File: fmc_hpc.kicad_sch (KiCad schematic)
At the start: 33 parts

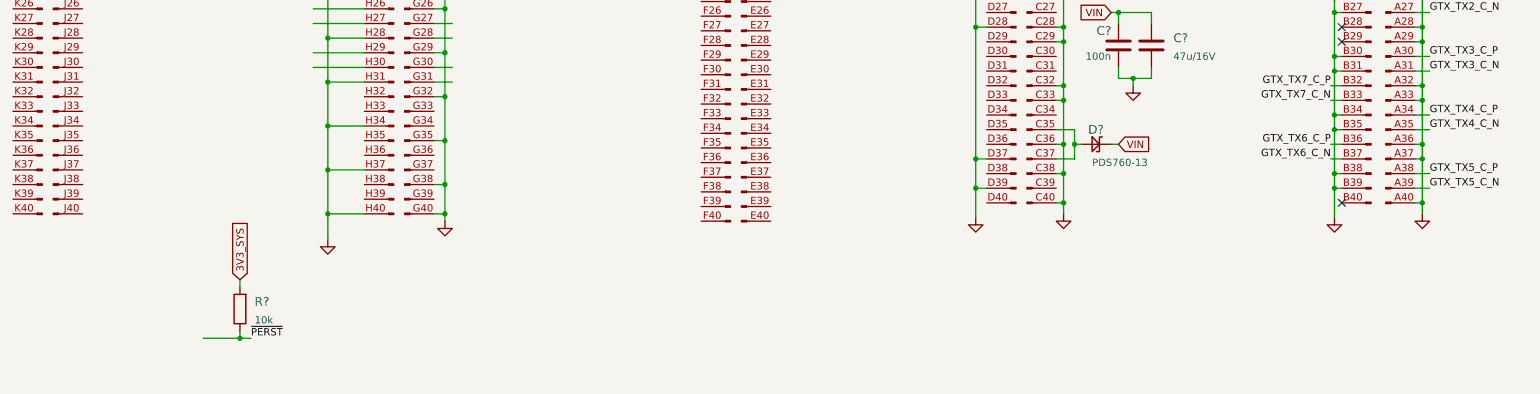
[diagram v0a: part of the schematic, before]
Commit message: Add power cycling circuitry
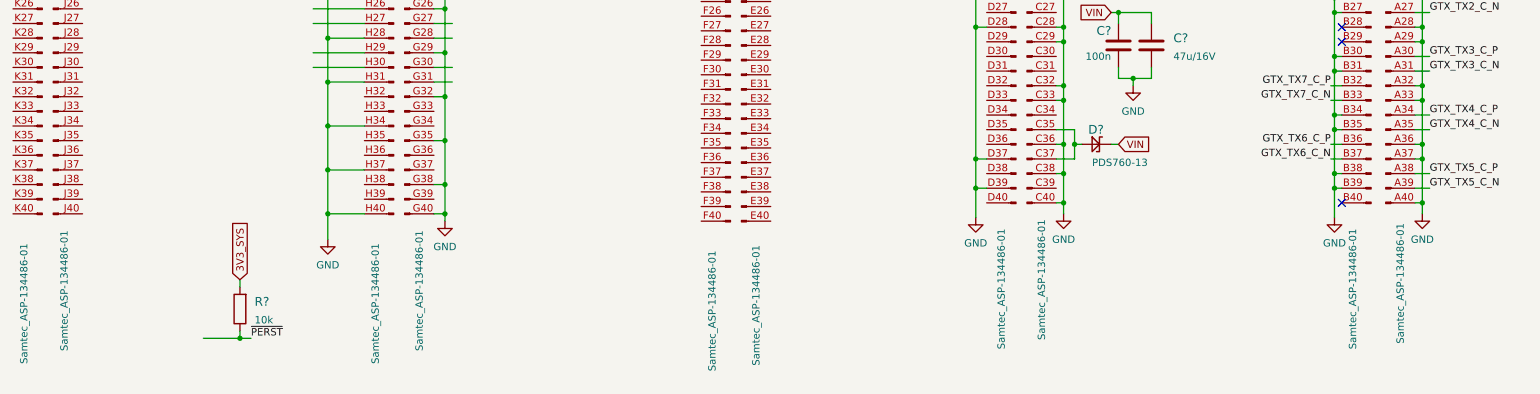
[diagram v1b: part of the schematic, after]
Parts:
- C? (x16): value (none) -> C_100n_0402; footprint (none) -> antmicro-footprints:0402-cap
- C?: value (none) -> C_100n_0201; footprint (none) -> antmicro-footprints:0201-res
- C?: value (none) -> C_47u_16V_1206; footprint (none) -> antmicro-footprints:1206-cap
- D?: value (none) -> PDS760-13; footprint (none) -> data-center-dram-tester-footprints:PDS760-13
- J? (x10): value (none) -> Samtec_ASP-134486-01
- R? (x2): value (none) -> R_33R_0402; footprint (none) -> antmicro-footprints:0402-res
- R?: value (none) -> R_10k_0402; footprint (none) -> antmicro-footprints:0402-res
- R?: value (none) -> R_100k_0402; footprint (none) -> antmicro-footprints:0402-res

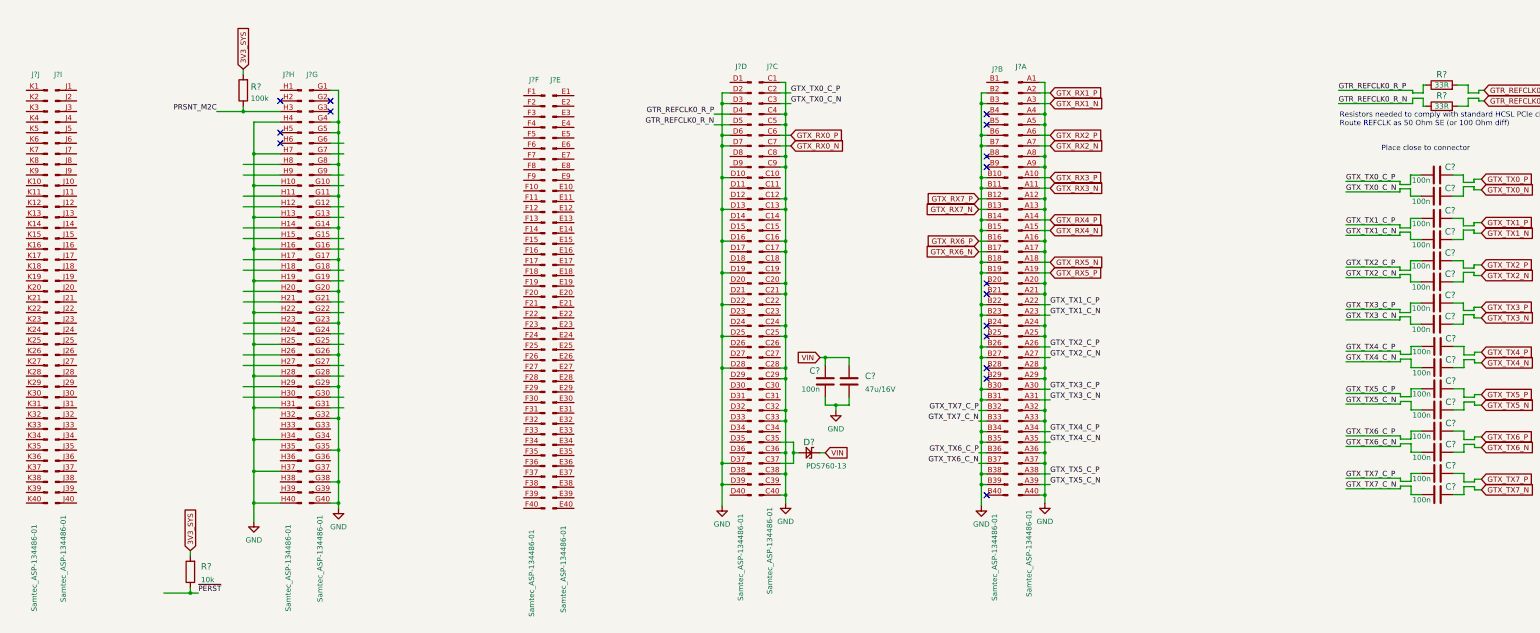
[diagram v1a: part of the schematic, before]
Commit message: Connect ETH mux, connect AUX_JTAG to FMC connector, add RC filter for HOT_SWAP_BUTTON signal
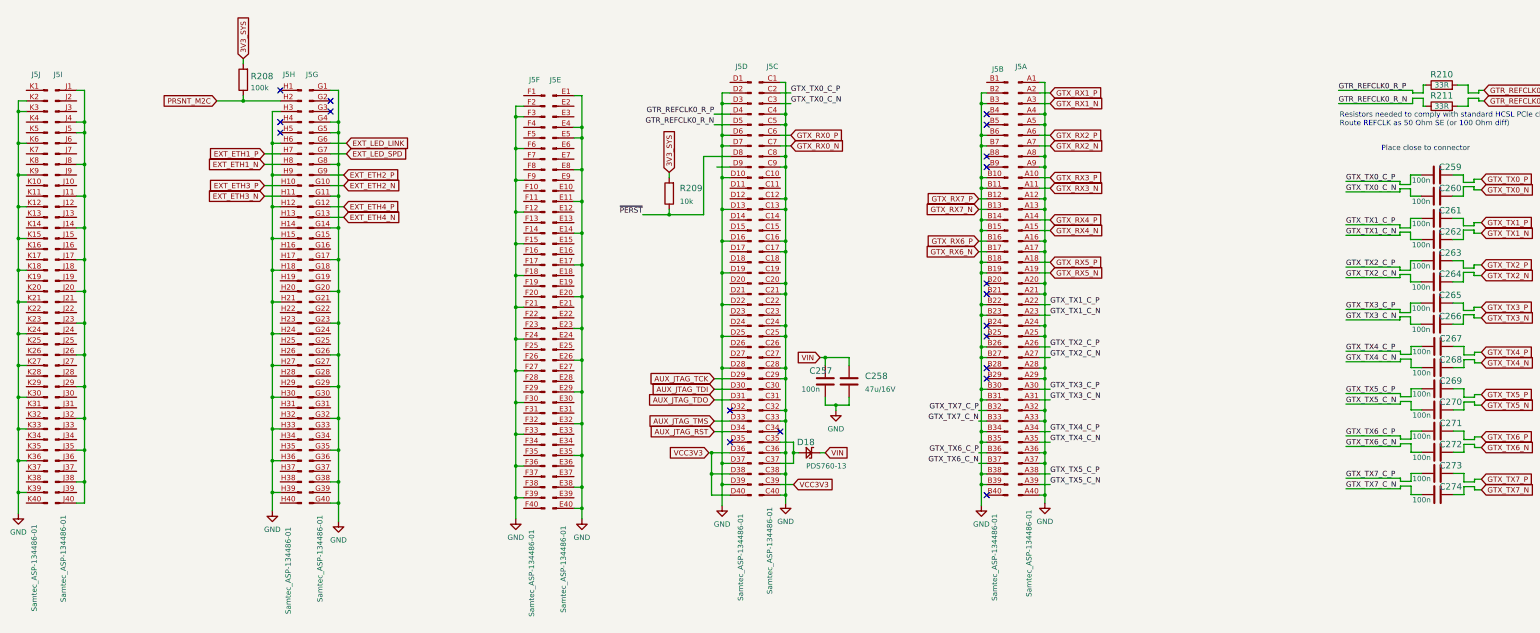
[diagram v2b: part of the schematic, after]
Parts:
- gave numbers to parts that had none: 24
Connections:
- net GND: now also J5.E1 (Pin_1), J5.E11 (Pin_11), J5.E14 (Pin_14), J5.E17 (Pin_17), J5.E20 (Pin_20), J5.E23 (Pin_23), J5.E26 (Pin_26), J5.E29 (Pin_29), J5.E32 (Pin_32), J5.E35 (Pin_35), J5.E38 (Pin_38), J5.E4 (Pin_4), J5.E40 (Pin_40), J5.E5 (Pin_5), J5.E8 (Pin_8), J5.F12 (Pin_12), J5.F15 (Pin_15), J5.F18 (Pin_18), J5.F2 (Pin_2), J5.F21 (Pin_21), J5.F24 (Pin_24), J5.F27 (Pin_27), J5.F3 (Pin_3), J5.F30 (Pin_30), J5.F33 (Pin_33), J5.F36 (Pin_36), J5.F39 (Pin_39), J5.F6 (Pin_6), J5.F9 (Pin_9), J5.H12 (Pin_12), J5.H15 (Pin_15), J5.H18 (Pin_18), J5.H21 (Pin_21), J5.H24 (Pin_24), J5.H27 (Pin_27), J5.H3 (Pin_3), J5.H30 (Pin_30), J5.H33 (Pin_33), J5.H36 (Pin_36), J5.H39 (Pin_39), J5.H6 (Pin_6), J5.H9 (Pin_9), J5.K12 (Pin_12), J5.K15 (Pin_15), J5.K18 (Pin_18), J5.K2 (Pin_2), J5.K21 (Pin_21), J5.K24 (Pin_24), J5.K27 (Pin_27), J5.K3 (Pin_3), J5.K30 (Pin_30), J5.K33 (Pin_33), J5.K36 (Pin_36), J5.K39 (Pin_39), J5.K6 (Pin_6), J5.K9 (Pin_9); no longer J5.H10 (Pin_10), J5.H13 (Pin_13), J5.H16 (Pin_16), J5.H19 (Pin_19), J5.H22 (Pin_22), J5.H25 (Pin_25), J5.H28 (Pin_28), J5.H31 (Pin_31), J5.H34 (Pin_34), J5.H37 (Pin_37), J5.H4 (Pin_4), J5.H40 (Pin_40), J5.H7 (Pin_7)
- net GTX_RX5_N: now also J5.A19 (Pin_19); no longer J5.A18 (Pin_18)
- net GTX_RX5_P: now also J5.A18 (Pin_18); no longer J5.A19 (Pin_19)
- net PRSNT_M2C: now also J5.H2 (Pin_2); no longer J5.H3 (Pin_3)
- net ~{PERST}: now also J5.D8 (Pin_8)
- net EXT_ETH3_N: now reaches J5.H11 (Pin_11)
- net EXT_ETH1_N: now reaches J5.H8 (Pin_8)
- net AUX_JTAG_TCK: now reaches J5.D29 (Pin_29)
- net AUX_JTAG_TDI: now reaches J5.D30 (Pin_30)
- net AUX_JTAG_TDO: now reaches J5.D31 (Pin_31)
- net AUX_JTAG_TMS: now reaches J5.D33 (Pin_33)
- net AUX_JTAG_RST: now reaches J5.D34 (Pin_34)
- net VCC3V3: now reaches J5.D36 (Pin_36)
- net VCC3V3: now also J5.C39 (Pin_39), J5.D38 (Pin_38), J5.D40 (Pin_40)
- net at J5.J1 (Pin_1): now also J5.J11 (Pin_11), J5.J14 (Pin_14), J5.J17 (Pin_17), J5.J20 (Pin_20), J5.J23 (Pin_23), J5.J26 (Pin_26), J5.J29 (Pin_29), J5.J32 (Pin_32), J5.J35 (Pin_35), J5.J38 (Pin_38), J5.J4 (Pin_4), J5.J40 (Pin_40), J5.J5 (Pin_5), J5.J8 (Pin_8)
- net EXT_ETH2_N: now reaches J5.G10 (Pin_10)
- net EXT_ETH4_P: now reaches J5.G12 (Pin_12)
- net EXT_ETH4_N: now reaches J5.G13 (Pin_13)
- net EXT_LED_LINK: now reaches J5.G6 (Pin_6)
- net EXT_LED_SPD: now reaches J5.G7 (Pin_7)
- net EXT_ETH2_P: now reaches J5.G9 (Pin_9)
- new net EXT_ETH1_P: J5.H7 (Pin_7)
- new net EXT_ETH3_P: J5.H10 (Pin_10)
- no-connect marks 16 -> 19
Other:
- moved on the sheet: R208, R209

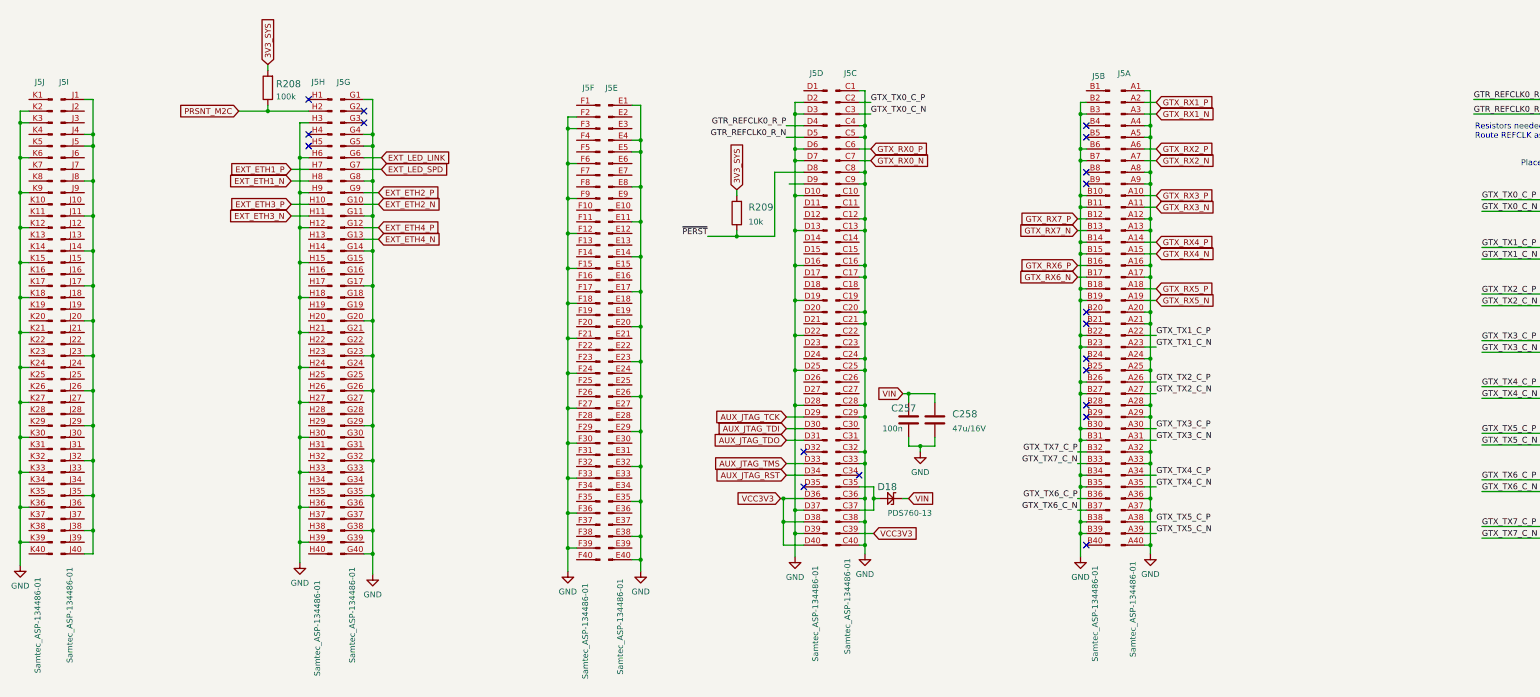
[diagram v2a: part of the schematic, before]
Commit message: Replaced JTAG to surface mount, Update FMC HPC socket
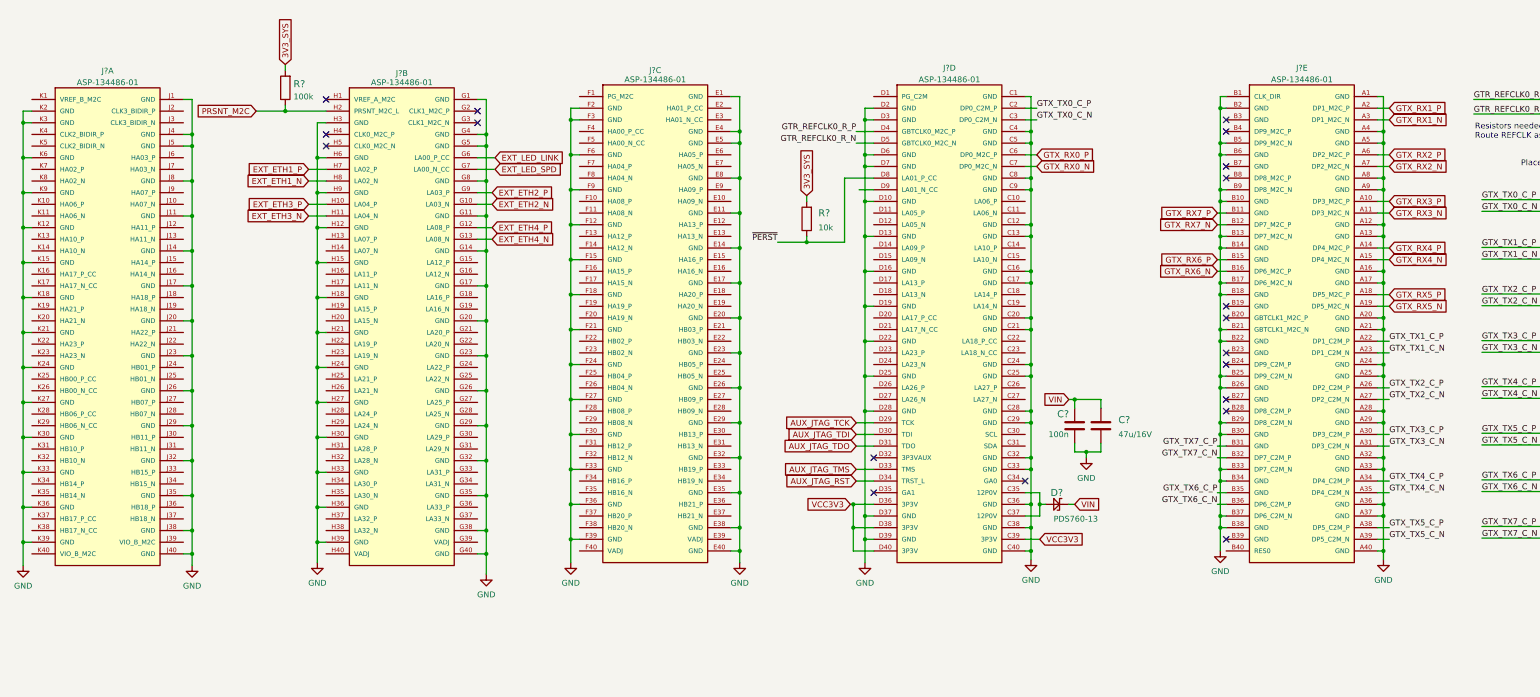
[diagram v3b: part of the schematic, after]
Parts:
- removed C257: C_100n_0201, antmicro-footprints:0201-res, symbol antmicroCapacitorsmisc:C_100n_0201
- removed C258: C_47u_16V_1206, antmicro-footprints:1206-cap, symbol antmicroCapacitorsmisc:C_47u_16V_1206
- removed D18: PDS760-13, data-center-dram-tester-footprints:PDS760-13, symbol data-center-dram-tester:PDS760-13
- removed J5: Samtec_ASP-134486-01, symbol Connector:Samtec_ASP-134486-01
- removed R208: R_100k_0402, antmicro-footprints:0402-res, symbol antmicroResistors0402:R_100k_0402
- removed R209: R_10k_0402, antmicro-footprints:0402-res, symbol antmicroResistors0402:R_10k_0402
- added C?: C_100n_0201, antmicro-footprints:0201-res, symbol antmicroCapacitorsmisc:C_100n_0201
- added C?: C_47u_16V_1206, antmicro-footprints:1206-cap, symbol antmicroCapacitorsmisc:C_47u_16V_1206
- added D?: PDS760-13, data-center-dram-tester-footprints:PDS760-13, symbol data-center-dram-tester:PDS760-13
- added J? (x5): ASP-134486-01, antmicro-footprints:SAMTEC_ASP-134486-01, symbol antmicroFMCConnectors:ASP-134486-01
- added R?: R_10k_0402, antmicro-footprints:0402-res, symbol antmicroResistors0402:R_10k_0402
- added R?: R_100k_0402, antmicro-footprints:0402-res, symbol antmicroResistors0402:R_100k_0402
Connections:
- net 3V3_SYS: now also R?.2, R?.2
- net AUX_JTAG_RST: now also J?.D34 (TRST_L)
- net AUX_JTAG_TCK: now also J?.D29 (TCK)
- net AUX_JTAG_TDI: now also J?.D30 (TDI)
- net AUX_JTAG_TDO: now also J?.D31 (TDO)
- net AUX_JTAG_TMS: now also J?.D33 (TMS)
- net EXT_ETH1_N: now also J?.H8 (LA02_N)
- net EXT_ETH1_P: now also J?.H7 (LA02_P)
- net EXT_ETH2_N: now also J?.G10 (LA03_N)
- net EXT_ETH2_P: now also J?.G9 (LA03_P)
- net EXT_ETH3_N: now also J?.H11 (LA04_N)
- net EXT_ETH3_P: now also J?.H10 (LA04_P)
- net EXT_ETH4_N: now also J?.G13 (LA08_N)
- net EXT_ETH4_P: now also J?.G12 (LA08_P)
- net EXT_LED_LINK: now also J?.G6 (LA00_P_CC)
- net EXT_LED_SPD: now also J?.G7 (LA00_N_CC)
- net GND: now also C?.2, C?.2, J?.A1 (GND), J?.A12 (GND), J?.A13 (GND), J?.A16 (GND), J?.A17 (GND), J?.A20 (GND), J?.A21 (GND), J?.A24 (GND), J?.A25 (GND), J?.A28 (GND), J?.A29 (GND), J?.A32 (GND), J?.A33 (GND), J?.A36 (GND), J?.A37 (GND), J?.A4 (GND), J?.A40 (GND), J?.A5 (GND), J?.A8 (GND), J?.A9 (GND), J?.B1 (CLK_DIR), J?.B10 (GND), J?.B13 (DP7_M2C_N), J?.B14 (GND), J?.B17 (DP6_M2C_N), J?.B18 (GND), J?.B2 (GND), J?.B21 (GBTCLK1_M2C_N), J?.B22 (GND), J?.B25 (DP9_C2M_N), J?.B26 (GND), J?.B29 (DP8_C2M_N), J?.B30 (GND), J?.B33 (DP7_C2M_N), J?.B34 (GND), J?.B37 (DP6_C2M_N), J?.B38 (GND), J?.B5 (DP9_M2C_N), J?.B6 (GND), J?.B9 (DP8_M2C_N), J?.C1 (GND), J?.C12 (GND), J?.C13 (GND), J?.C16 (GND), J?.C17 (GND), J?.C20 (GND), J?.C21 (GND), J?.C24 (GND), J?.C25 (GND), J?.C28 (GND), J?.C29 (GND), J?.C32 (GND), J?.C33 (GND), J?.C36 (GND), J?.C38 (GND), J?.C4 (GND), J?.C40 (GND), J?.C5 (GND), J?.C8 (GND), J?.C9 (GND), J?.D10 (GND), J?.D13 (GND), J?.D16 (GND), J?.D19 (GND), J?.D2 (GND), J?.D22 (GND), J?.D25 (GND), J?.D28 (GND), J?.D3 (GND), J?.D37 (GND), J?.D39 (GND), J?.D6 (GND), J?.D7 (GND), J?.E1 (GND), J?.E11 (GND), J?.E14 (GND), J?.E17 (GND), J?.E20 (GND), J?.E23 (GND), J?.E26 (GND), J?.E29 (GND), J?.E32 (GND), J?.E35 (GND), J?.E38 (GND), J?.E4 (GND), J?.E40 (GND), J?.E5 (GND), J?.E8 (GND), J?.F12 (GND), J?.F15 (GND), J?.F18 (GND), J?.F2 (GND), J?.F21 (GND), J?.F24 (GND), J?.F27 (GND), J?.F3 (GND), J?.F30 (GND), J?.F33 (GND), J?.F36 (GND), J?.F39 (GND), J?.F6 (GND), J?.F9 (GND), J?.G1 (GND), J?.G11 (GND), J?.G14 (GND), J?.G17 (GND), J?.G20 (GND), J?.G23 (GND), J?.G26 (GND), J?.G29 (GND), J?.G32 (GND), J?.G35 (GND), J?.G38 (GND), J?.G4 (GND), J?.G40 (GND), J?.G5 (GND), J?.G8 (GND), J?.H12 (GND), J?.H15 (GND), J?.H18 (GND), J?.H21 (GND), J?.H24 (GND), J?.H27 (GND), J?.H3 (GND), J?.H30 (GND), J?.H33 (GND), J?.H36 (GND), J?.H39 (GND), J?.H6 (GND), J?.H9 (GND), J?.J1 (GND), J?.J11 (GND), J?.J14 (GND), J?.J17 (GND), J?.J20 (GND), J?.J23 (GND), J?.J26 (GND), J?.J29 (GND), J?.J32 (GND), J?.J35 (GND), J?.J38 (GND), J?.J4 (GND), J?.J40 (GND), J?.J5 (GND), J?.J8 (GND), J?.K12 (GND), J?.K15 (GND), J?.K18 (GND), J?.K2 (GND), J?.K21 (GND), J?.K24 (GND), J?.K27 (GND), J?.K3 (GND), J?.K30 (GND), J?.K33 (GND), J?.K36 (GND), J?.K39 (GND), J?.K6 (GND), J?.K9 (GND)
- net GTR_REFCLK0_R_N: now also J?.D5 (GBTCLK0_M2C_N)
- net GTR_REFCLK0_R_P: now also J?.D4 (GBTCLK0_M2C_P)
- net GTX_RX0_N: now also J?.C7 (DP0_M2C_N)
- net GTX_RX0_P: now also J?.C6 (DP0_M2C_P)
- net GTX_RX1_N: now also J?.A3 (DP1_M2C_N)
- net GTX_RX1_P: now also J?.A2 (DP1_M2C_P)
- net GTX_RX2_N: now also J?.A7 (DP2_M2C_N)
- net GTX_RX2_P: now also J?.A6 (DP2_M2C_P)
- net GTX_RX3_N: now also J?.A11 (DP3_M2C_N)
- net GTX_RX3_P: now also J?.A10 (DP3_M2C_P)
- net GTX_RX4_N: now also J?.A15 (DP4_M2C_N)
- net GTX_RX4_P: now also J?.A14 (DP4_M2C_P)
- net GTX_RX5_N: now also J?.A19 (DP5_M2C_N)
- net GTX_RX5_P: now also J?.A18 (DP5_M2C_P)
- net GTX_RX6_N: now also J?.B16 (DP6_M2C_P)
- net GTX_RX6_P: now also J?.B15 (GND)
- net GTX_RX7_N: now also J?.B12 (DP7_M2C_P)
- net GTX_RX7_P: now also J?.B11 (GND)
- net GTX_TX0_C_N: now also J?.C3 (DP0_C2M_N)
- net GTX_TX0_C_P: now also J?.C2 (DP0_C2M_P)
- net GTX_TX1_C_N: now also J?.A23 (DP1_C2M_N)
- net GTX_TX1_C_P: now also J?.A22 (DP1_C2M_P)
- net GTX_TX2_C_N: now also J?.A27 (DP2_C2M_N)
- net GTX_TX2_C_P: now also J?.A26 (DP2_C2M_P)
- net GTX_TX3_C_N: now also J?.A31 (DP3_C2M_N)
- net GTX_TX3_C_P: now also J?.A30 (DP3_C2M_P)
- net GTX_TX4_C_N: now also J?.A35 (DP4_C2M_N)
- net GTX_TX4_C_P: now also J?.A34 (DP4_C2M_P)
- net GTX_TX5_C_N: now also J?.A39 (DP5_C2M_N)
- net GTX_TX5_C_P: now also J?.A38 (DP5_C2M_P)
- net GTX_TX6_C_N: now also J?.B36 (DP6_C2M_P)
- net GTX_TX6_C_P: now also J?.B35 (GND)
- net GTX_TX7_C_N: now also J?.B32 (DP7_C2M_P)
- net GTX_TX7_C_P: now also J?.B31 (GND)
- net PRSNT_M2C: now also J?.H2 (PRSNT_M2C_L), R?.1
- net VCC3V3: now also J?.C39 (3P3V), J?.D36 (3P3V), J?.D38 (3P3V), J?.D40 (3P3V)
- net VIN: now also C?.1, C?.1, D?.C
- net ~{PERST}: now also J?.D8 (LA01_P_CC), R?.1
- new net: D?.A, J?.C35 (12P0V), J?.C37 (12P0V)
